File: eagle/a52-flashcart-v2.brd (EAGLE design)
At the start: 50.8 x 50.8 mm, 11 parts

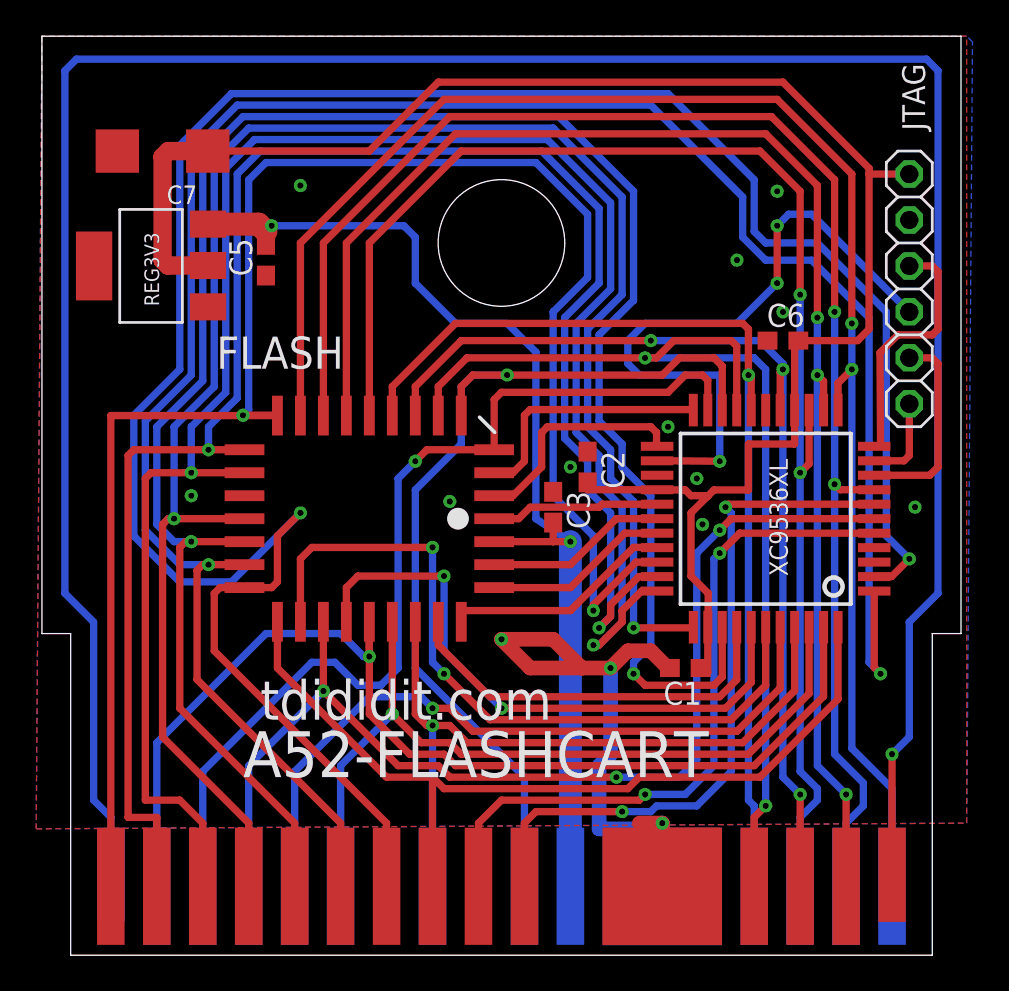
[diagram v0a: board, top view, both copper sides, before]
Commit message: board update - PHI2 signal connected to CPLD
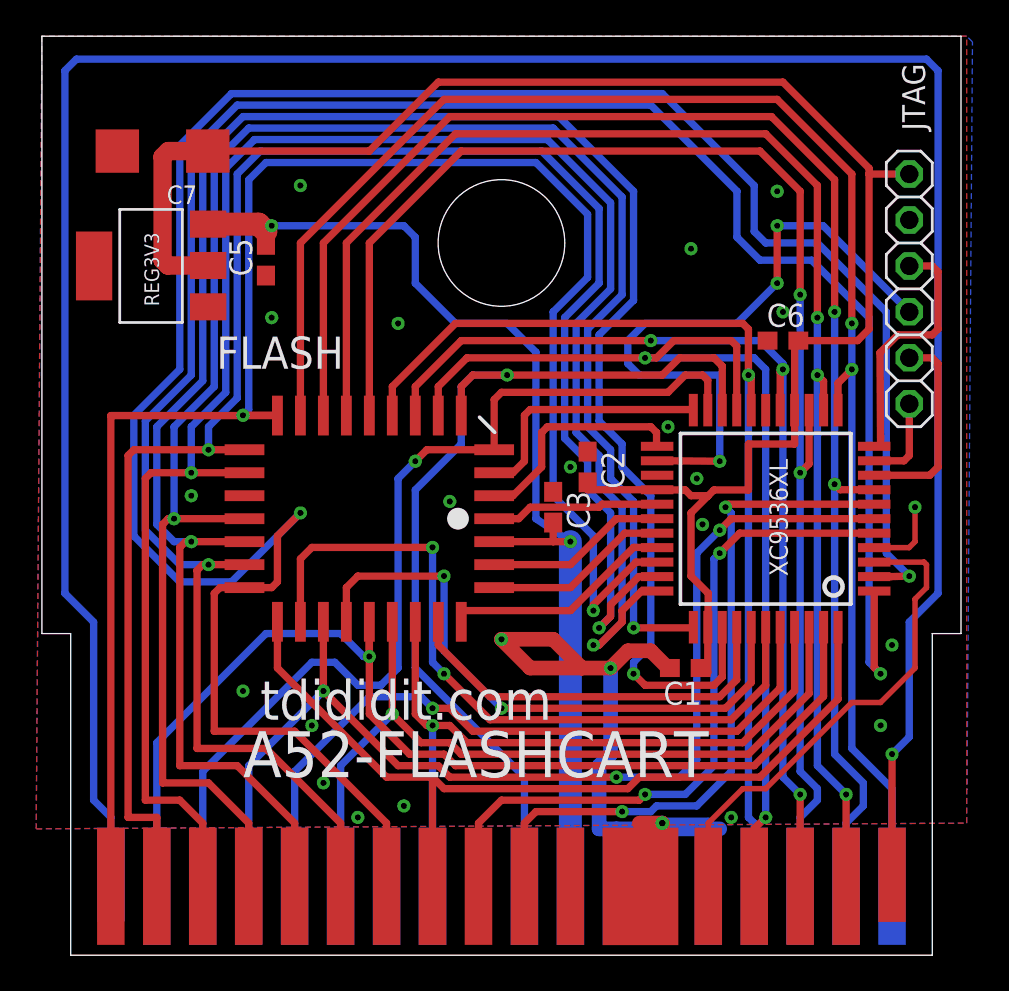
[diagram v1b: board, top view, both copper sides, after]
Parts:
- U$1: value ATARI-5200S -> ATARI-5200-TS; device a52-cartridge:ATARI-5200-SMALL -> a52-cartridge:ATARI-5200-SMALL-T
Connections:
- new net PHI2: U$1.14, XC9536XL.3
- net GND: now also U$1.23, U$1.25
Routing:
- net PHI2: track 0.00 -> 27.4 mm
- net GND: track 36.9 -> 58.1 mm, vias 14 -> 25
- net D6: track 126.1 -> 129.1 mm
- net D5: track 119.1 -> 121.6 mm
- net D4: track 112.3 -> 114.2 mm
- net D3: track 101.1 -> 102.6 mm
- net TDO: track 37.4 -> 36.9 mm
